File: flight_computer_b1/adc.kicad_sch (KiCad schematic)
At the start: 0 parts

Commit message: flight computer updates
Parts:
- added C10, C11: 4.7pf, Capacitor_SMD:C_0603_1608Metric, symbol Device:C
- added C5, C8: 0.1uF, Capacitor_SMD:C_0603_1608Metric, symbol Device:C
- added C6: 10uF, Capacitor_SMD:C_0603_1608Metric, symbol Device:C
- added C7: 10uF, Capacitor_SMD:C_0603_1608Metric, symbol Device:C_Polarized
- added C9: 22nf, Capacitor_SMD:C_0603_1608Metric, symbol Device:C
- added D1: LED, Capacitor_SMD:C_0603_1608Metric, symbol Device:LED
- added R40: 100, Resistor_SMD:R_0603_1608Metric, symbol Device:R_US
- added U6: ADS1158IRTCR, RTC0048A-IPC_A, symbol avi_lib:ADS1158IRTCR
- added Y1: 32.768kHz, avi_lib:XTAL_MC-306_32.7680K-A0_ROHS, symbol avi_lib:MC-306_32.7680K-A0_ROHS
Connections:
- net AINCOM: now also U6.32 (AINCOM)
- net CS: now also U6.27 (CS_N)
- net DIN: now also U6.23 (DIN)
- net DOUT: now also U6.24 (DOUT)
- net DVDD: now also U6.10 (PWDN_N), U6.11 (RESET_N), U6.26 (START)
- net GPIO0: now also U6.14 (GPIO0)
- net GPIO1: now also U6.15 (GPIO1)
- net GPIO2: now also U6.16 (GPIO2)
- net GPIO3: now also U6.17 (GPIO3)
- net GPIO4: now also U6.18 (GPIO4)
- net GPIO5: now also U6.19 (GPIO5)
- net GPIO6: now also U6.20 (GPIO6)
- net GPIO7: now also U6.21 (GPIO7)
- net IN0: now also U6.4 (AIN0)
- net IN1: now also U6.3 (AIN1)
- net IN10: now also U6.38 (AIN10)
- net IN11: now also U6.37 (AIN11)
- net IN12: now also U6.36 (AIN12)
- net IN13: now also U6.35 (AIN13)
- net IN14: now also U6.34 (AIN14)
- net IN15: now also U6.33 (AIN15)
- net IN2: now also U6.2 (AIN2)
- net IN3: now also U6.1 (AIN3)
- net IN4: now also U6.48 (AIN4)
- net IN5: now also U6.47 (AIN5)
- net IN6: now also U6.46 (AIN6)
- net IN7: now also U6.45 (AIN7)
- net IN8: now also U6.40 (AIN8)
- net IN9: now also U6.39 (AIN9)
- net SCLK: now also U6.22 (SCLK)
- new net: D1.2 (A), R40.2
- new net: C11.2, U6.9 (XTAL2), Y1.4
- new net: C9.2, U6.7 (PLLCAP)
- new net: C10.2, U6.8 (XTAL1), Y1.1
- new net: Y1.2 (NC), Y1.3 (NC__1)
- new net +5V: C5.1, C6.1, C7.1, C8.1, R40.1, U6.28 (DVDD), U6.31 (VREFP), U6.6 (AVDD)
- new net GND: C10.1, C11.1, C5.2, C6.2, C7.2, C8.2, C9.1, D1.1 (K), U6.12 (CLKSEL), U6.29 (DGND), U6.30 (VREFN), U6.49 (EP), U6.5 (AVSS)
- no-connect marks 0 -> 6

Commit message: flight computer changes
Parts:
- added U8, U9: MCP6001-OT, Package_TO_SOT_SMD:SOT-23-5, symbol Amplifier_Operational:MCP6001-OT
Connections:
- net DGND: now also U8.2 (V-), U9.2 (V-)
- net DVDD: now also U8.5 (V+), U9.5 (V+)
- net ADCINN: now reaches U6.41 (ADCINN)
- net ADCINN: now also U9.1, U9.4 (-)
- net ADCINP: now reaches U6.42 (ADCINP)
- net ADCINP: now also U8.1, U8.4 (-)
- net MUXOUTN: now reaches U6.43 (MUXOUTN)
- net MUXOUTN: now also U9.3 (+)
- net MUXOUTP: now reaches U6.44 (MUXOUTP)
- net MUXOUTP: now also U8.3 (+)
- no-connect marks 6 -> 2
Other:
- moved on the sheet: C10, C11, C5, C6, C7, C8, C9, D1, R40, U6, Y1

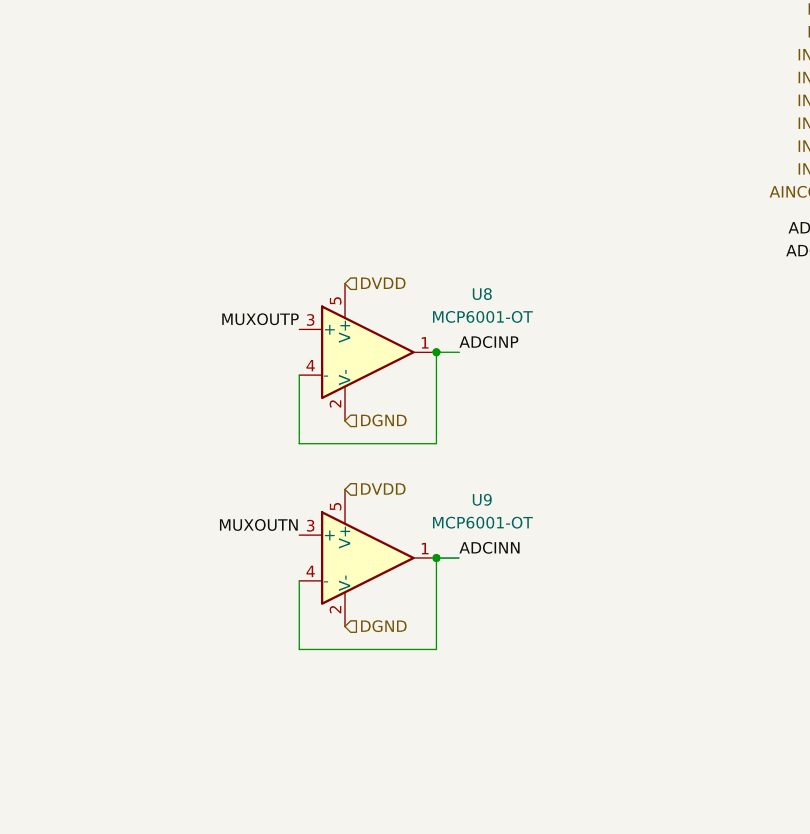
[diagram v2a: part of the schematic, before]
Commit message: flight computer: added mux and voltage sense channels
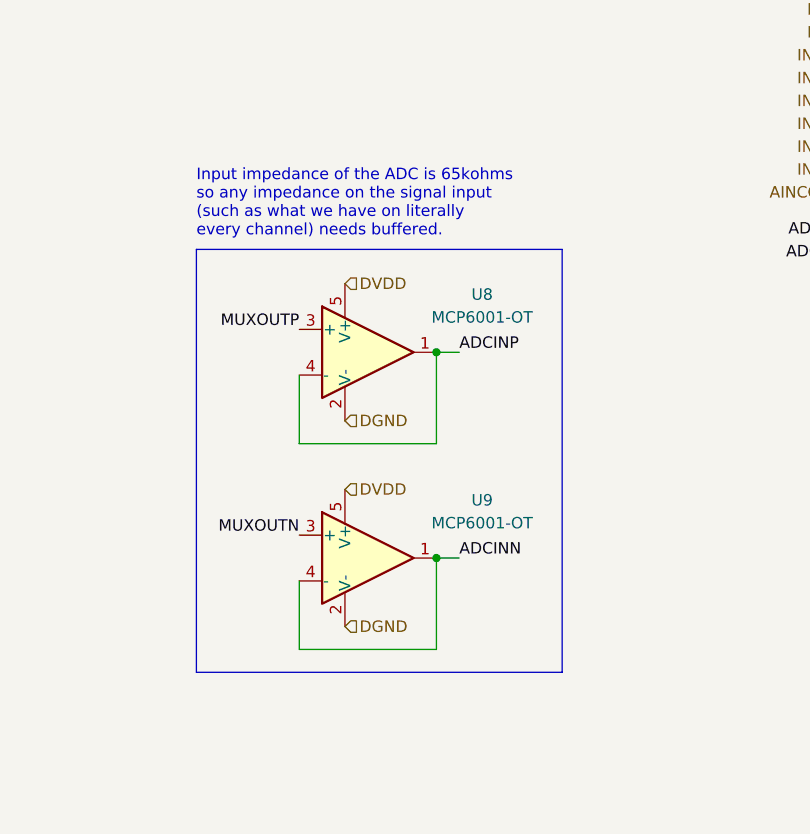
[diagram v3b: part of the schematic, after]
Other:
- note added: "Input impedance of the ADC is 65kohms so any impedance on the signal input (such as what we have on literally every channel) needs buffered."
- company: (none) -> Purdue Space Program Liquids
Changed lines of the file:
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@@
 	(generator_version "9.0")
 	(paper "A4")
+	(title_block
+		(date "2025-11-05")
+		(rev "1")
+		(company "Purdue Space Program Liquids")
+	)
+	(rectangle
+		(start 52.07 118.11)
+		(end 92.71 165.1)
+		(stroke
+			(width 0)
+			(type default)
+		)
+		(fill
+			(type none)
+		)
+	)
+	(text "Input impedance of the ADC is 65kohms\nso any impedance on the signal input\n(such as what we have on literally\nevery channel) needs buffered."
+		(exclude_from_sim no)
+		(at 52.07 113.03 0)
+		(effects
+			(font
+				(size 1.27 1.27)
+			)
+			(justify left)
+		)
+	)
 	(junction
 		(at 115.57 55.88)

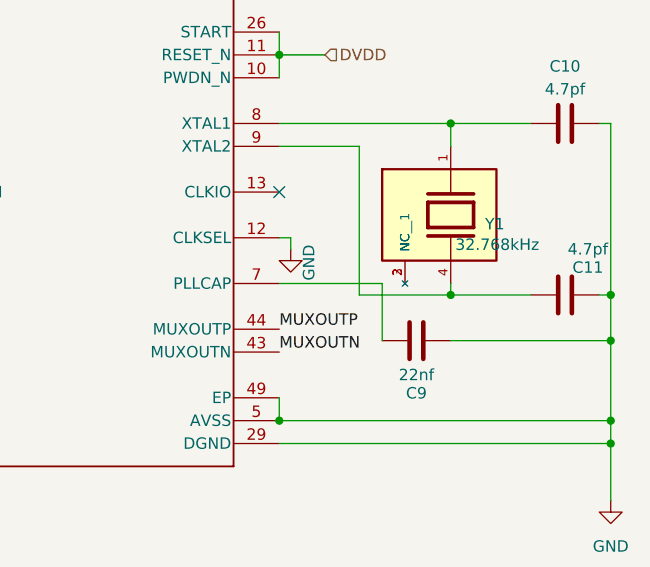
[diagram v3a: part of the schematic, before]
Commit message: flight computer: added pyro circuit and digikey part numbers
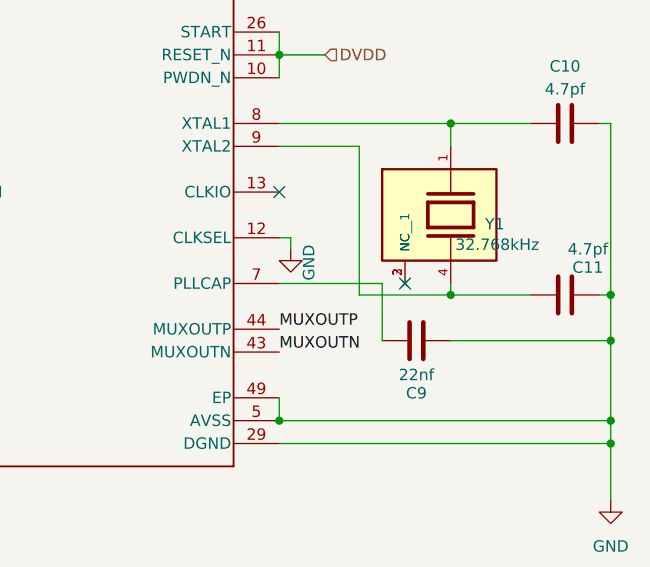
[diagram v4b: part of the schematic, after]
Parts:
- U6: DIGIKEY PART N (none) -> ADS1158IRTCR-ND
- U8, U9: DIGIKEY PART N (none) -> MCP6001T-I/OTCT-ND
- Y1: DIGIKEY PART N (none) -> SER2407CT-ND
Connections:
- no-connect marks 2 -> 3
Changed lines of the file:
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@@
+	)
+	(no_connect
+		(at 181.61 121.92)
 	)
 	(no_connect
@@
 		)
 		(property "Description" "Unpolarized capacitor"
+			(at 63.5 44.45 0)
+			(effects
+				(font
+					(size 1.27 1.27)
+				)
+				(hide yes)
+			)
+		)
+		(property "DIGIKEY PART N" ""
 			(at 63.5 44.45 0)
 			(effects
@@
 			)
 		)
+		(property "DIGIKEY PART N" ""
+			(at 45.72 55.88 90)
+			(effects
+				(font
+					(size 1.27 1.27)
+				)
+				(hide yes)
+			)
+		)
 		(pin "2"
 		)
@@
 		(property "Description" "Unpolarized capacitor"
 			(at 199.39 123.19 0)
+			(effects
+				(font
+					(size 1.27 1.27)
+				)
+				(hide yes)
+			)
+		)
+		(property "DIGIKEY PART N" ""
+			(at 199.39 123.19 90)
 			(effects
 				(font
@@
 			)
 		)
+		(property "DIGIKEY PART N" ""
+			(at 45.72 45.72 0)
+			(effects
+				(font
+					(size 1.27 1.27)
+				)
+				(hide yes)
+			)
+		)
 		(pin "1"
 		)
@@
 			)
 		)
+		(property "DIGIKEY PART N" "ADS1158IRTCR-ND"
+			(at 124.46 55.88 0)
+			(effects
+				(font
+					(size 1.27 1.27)
+				)
+				(hide yes)
+			)
+		)
 		(pin "46"
 		)
@@
 		(property "Description" "Unpolarized capacitor"
 			(at 199.39 104.14 0)
+			(effects
+				(font
+					(size 1.27 1.27)
+				)
+				(hide yes)
+			)
+		)
+		(property "DIGIKEY PART N" ""
+			(at 199.39 104.14 90)
 			(effects
 				(font
@@
 			)
 		)
+		(property "DIGIKEY PART N" ""
+			(at 73.66 44.45 0)
+			(effects
+				(font
+					(size 1.27 1.27)
+				)
+				(hide yes)
+			)
+		)
 		(pin "1"
 		)
@@
 			)
 		)
+		(property "DIGIKEY PART N" ""
+			(at 182.88 128.27 90)
+			(effects
+				(font
+					(size 1.27 1.27)
+				)
+				(hide yes)
+			)
+		)
 		(pin "1"
 		)
@@
 		)
 		(property "Description" "Unpolarized capacitor"
+			(at 106.68 62.23 0)
+			(effects
+				(font
+					(size 1.27 1.27)
+				)
+				(hide yes)
+			)
+		)
+		(property "DIGIKEY PART N" ""
 			(at 106.68 62.23 0)
 			(effects
@@
 			)
 		)
+		(property "DIGIKEY PART N" ""
+			(at 95.25 62.23 0)
+			(effects
+				(font
+					(size 1.27 1.27)
+				)
+				(hide yes)
+			)
+		)
 		(pin "1"
 		)
@@
 			)
 		)
+		(property "DIGIKEY PART N" "MCP6001T-I/OTCT-ND"
+			(at 71.12 152.4 0)
+			(effects
+				(font
+					(size 1.27 1.27)
+				)
+				(hide yes)
+			)
+		)
 		(pin "5"
 		)
@@
 			)
 		)
+		(property "DIGIKEY PART N" "MCP6001T-I/OTCT-ND"
+			(at 71.12 129.54 0)
+			(effects
+				(font
+					(size 1.27 1.27)
+				)
+				(hide yes)
+			)
+		)
 		(pin "5"
 		)
@@
 				(hide yes)
 			)
+		)
+		(property "DIGIKEY PART N" "SER2407CT-ND"
+			(at 186.69 114.3 90)
+			(effects
+				(font
+					(size 1.27 1.27)
+				)
+				(hide yes)
+			)

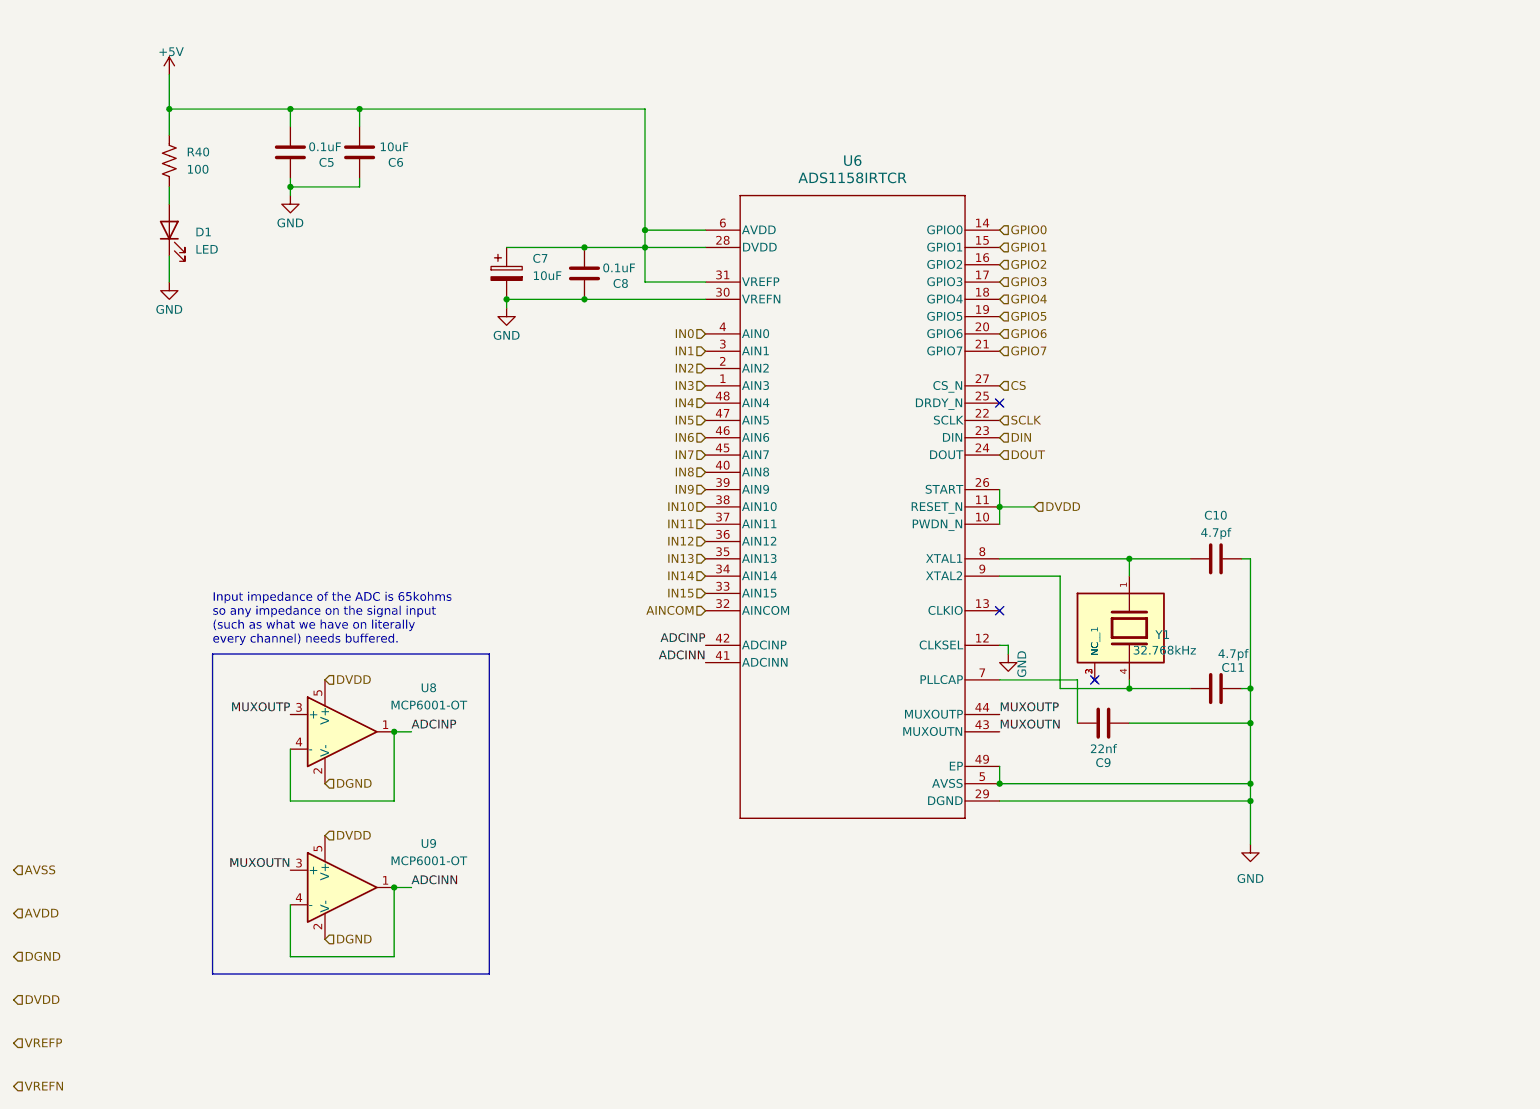
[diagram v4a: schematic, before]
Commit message: flight computer: routing updates
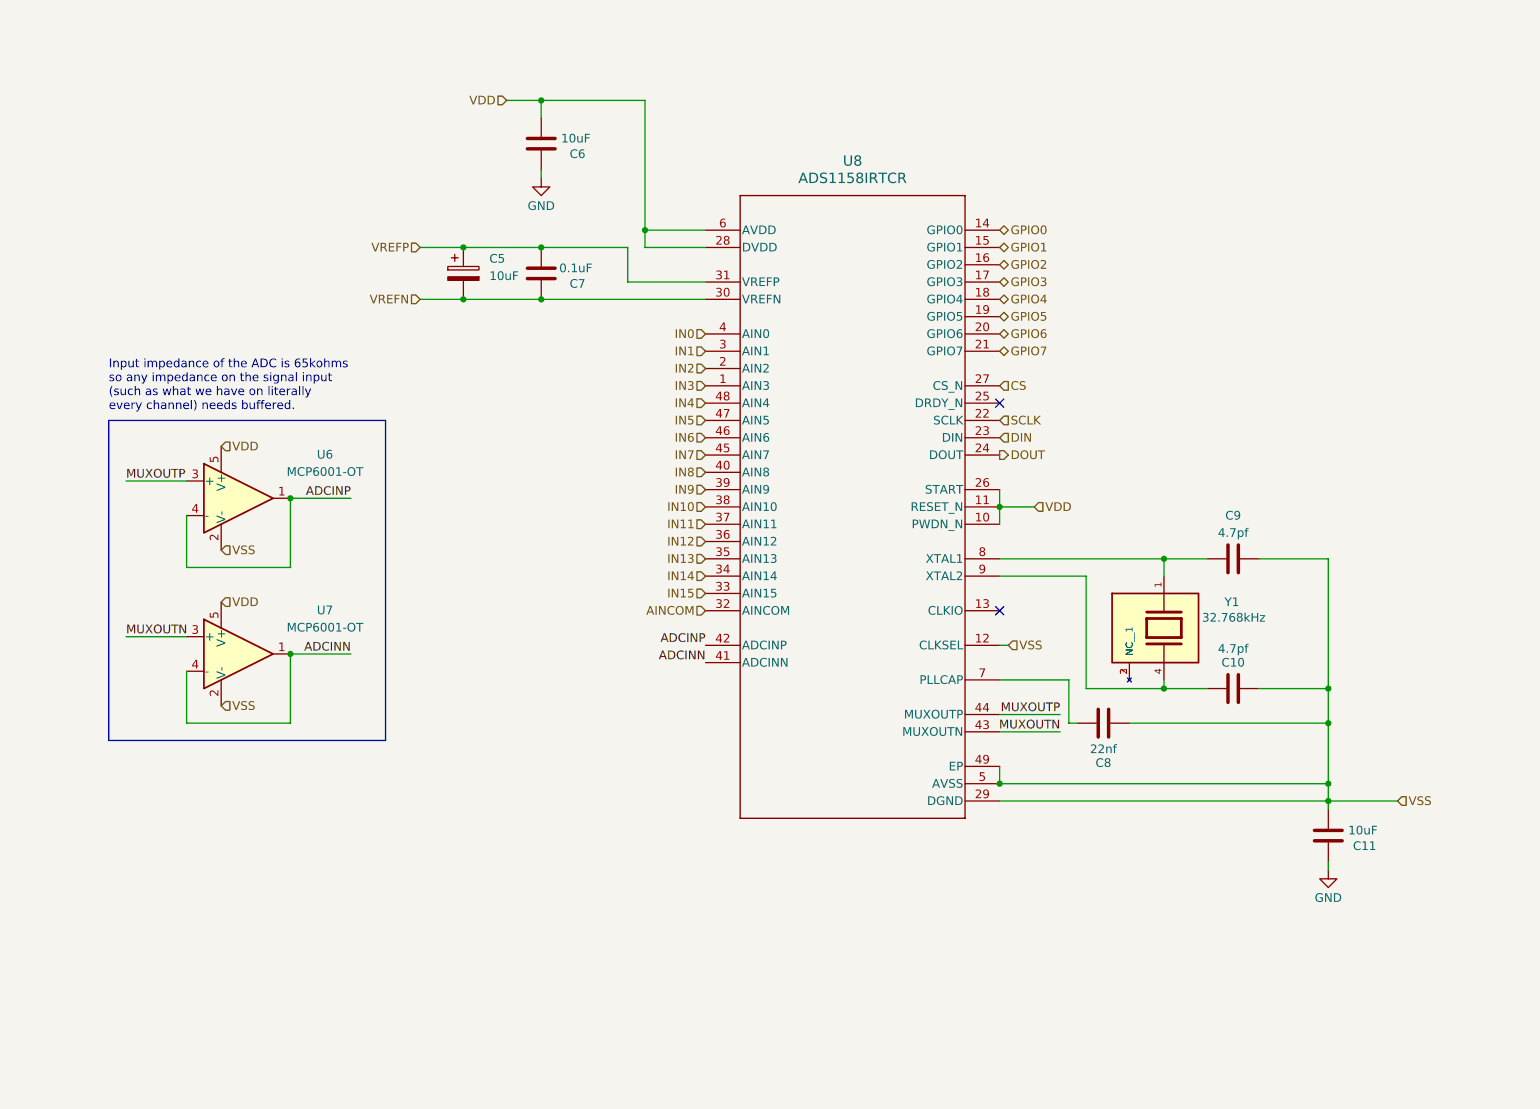
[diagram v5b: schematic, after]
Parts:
- removed C5: 0.1uF, Capacitor_SMD:C_0603_1608Metric, symbol Device:C
- removed D1: LED, Capacitor_SMD:C_0603_1608Metric, symbol Device:LED
- removed R40: 100, Resistor_SMD:R_0603_1608Metric, symbol Device:R_US
- added C11: 10uF, Capacitor_SMD:C_0603_1608Metric, symbol Device:C
- C5: renamed from C7; footprint Capacitor_SMD:C_0603_1608Metric -> Capacitor_SMD:C_0805_2012Metric; DIGIKEY PART N (none) -> 478-TCP0J106M8RCT-ND
- renumbered C11 to C10, C8 to C7, C9 to C8, C10 to C9, U8 to U6, U9 to U7, U6 to U8
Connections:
- net DVDD is gone; now on net VDD: U6.5 (V+), U7.5 (V+), U8.10 (PWDN_N), U8.11 (RESET_N), U8.26 (START)
- net GND: now also C11.2; no longer C10.1, C5.2, C7.2, C8.1, C9.1, U8.12 (CLKSEL), U8.29 (DGND), U8.30 (VREFN), U8.49 (EP), U8.5 (AVSS)
- net VREFN: now also C5.2, C7.2, U8.30 (VREFN)
- net VREFP: now also C5.1, C7.1, U8.31 (VREFP)
- net +5V renamed VDD
- net VDD: no longer C5.1, C7.1, U8.31 (VREFP)
- net DGND renamed VSS
- net VSS: now also C10.1, C8.1, C9.1, U8.12 (CLKSEL), U8.29 (DGND), U8.49 (EP), U8.5 (AVSS), C11.1
- no-connect marks 3 -> 2
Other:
- moved on the sheet: C10, C5, C6, C7, C9, U6, U7, Y1

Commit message: assigned footprints to capacitors
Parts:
- U8: footprint RTC0048A-IPC_A -> avi_footprint:RTC0048A-IPC_A
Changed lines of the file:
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@@
 			)
 		)
-		(property "Footprint" "RTC0048A-IPC_A"
+		(property "Footprint" "avi_footprint:RTC0048A-IPC_A"
 			(at 124.46 55.88 0)
 			(effects
